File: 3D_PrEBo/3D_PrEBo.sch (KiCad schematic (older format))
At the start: 69 parts, among them J1 LED, J10 FAN&LED_INPUT, J11 TMC_INPUT, J12 Fan_interconnection_header, J13 Conn_01x04, J14 Conn_01x03, J2 RJ45, J3 X, J4 Y, J5 Z, J6 E0, J7 E1, J9 X_endstop, M1 Fan_3pin, M2 Fan_3pin, M3 Fan_3pin, M4 Fan_3pin, M5 Fan_3pin, M6 Fan_3pin, M7 Fan_3pin, M8 Fan_4pin, Q1 AOD4189, Q10 IRLML2502, Q2 IRLML2502, Q3 IRLML2502, Q4 IRLML2502, Q5 IRLML2502, Q6 IRLML2502, Q7 IRLML2502, Q8 IRLML2502, Q9 IRLML2502, U1 L5973D, U2 NCP1117-5.0_SOT223

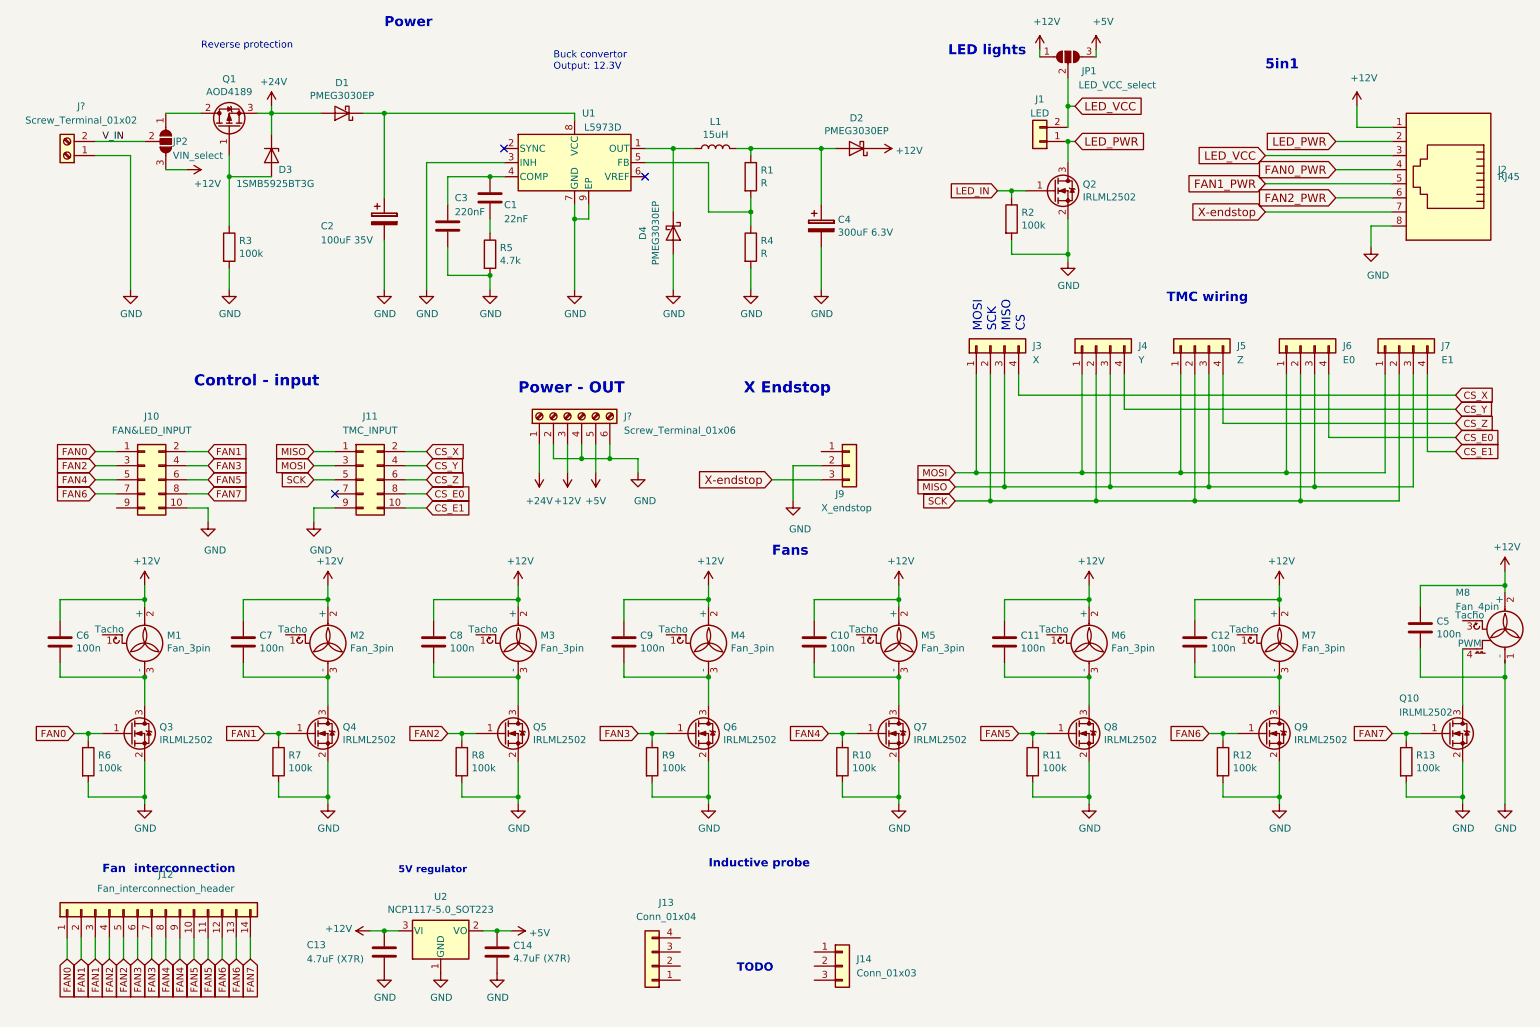
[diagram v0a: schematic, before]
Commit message: Schematic: Add inductive probe and set voltage of buck converter
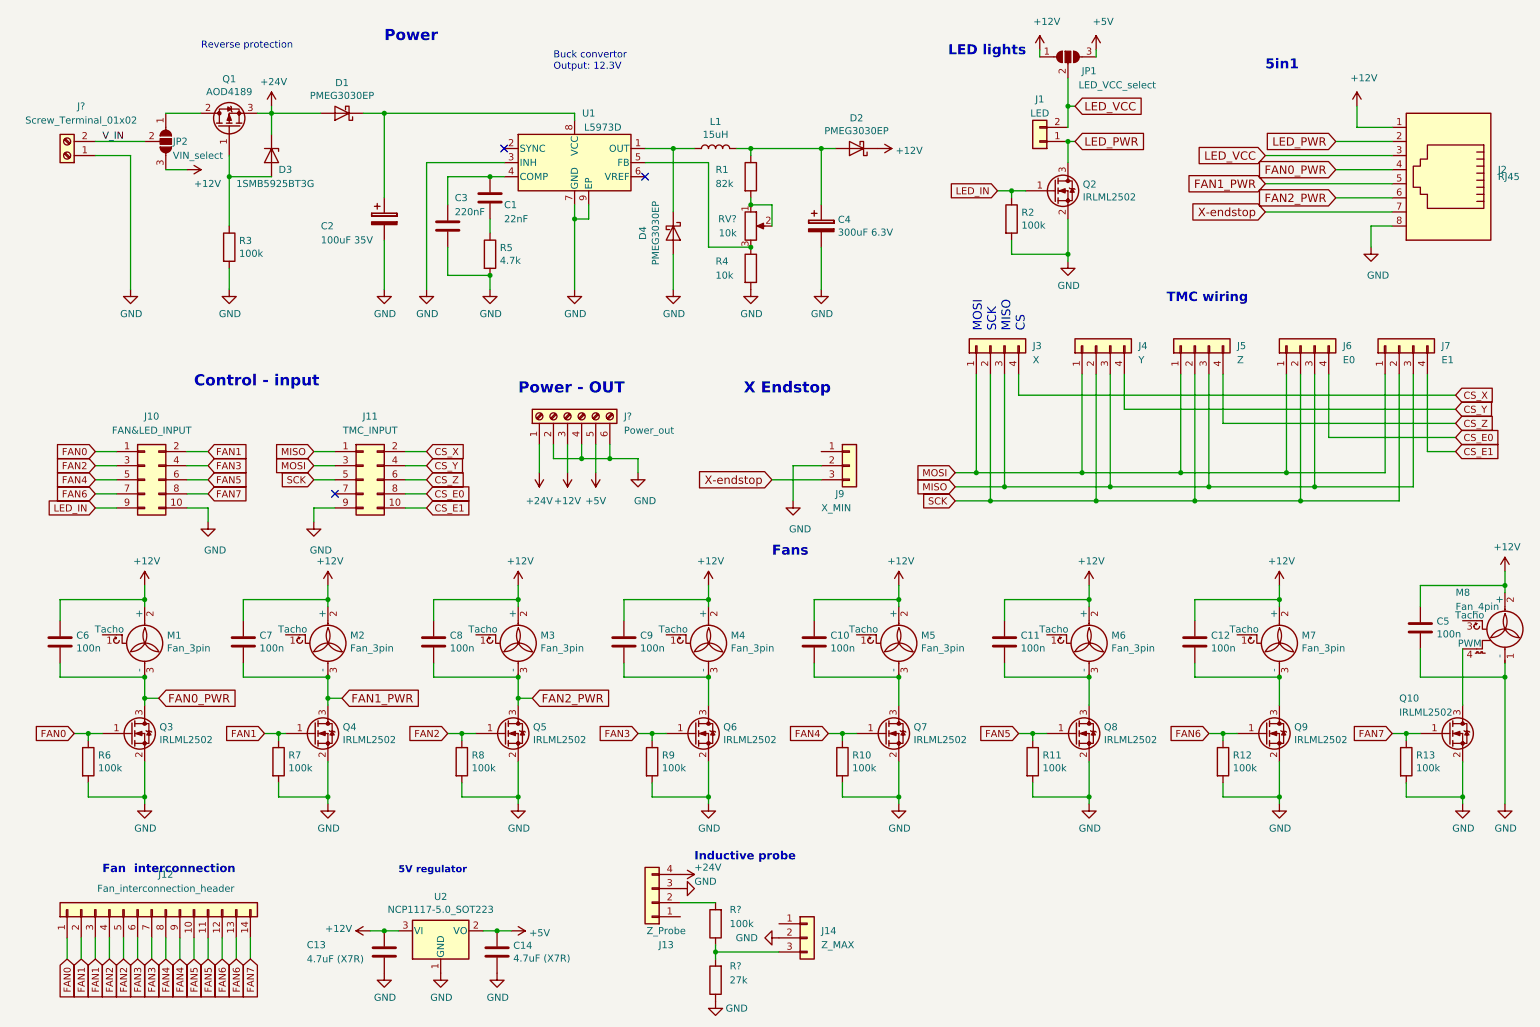
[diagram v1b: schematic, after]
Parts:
- added R?: 100k, symbol Device:R
- added R?: 27k, symbol Device:R
- added RV?: 10k, symbol Device:R_POT
- J13: value Conn_01x04 -> Z_Probe
- J14: value Conn_01x03 -> Z_MAX
- J9: value X_endstop -> X_MIN
- J?: value Screw_Terminal_01x06 -> Power_out
- R1: value R -> 82k
- R4: value R -> 10k
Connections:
- net +24V: now also J13.4 (Pin_4)
- net FAN0_PWR: now also C6.2, M1.3 (-), Q3.3 (D)
- net FAN1_PWR: now also C7.2, M2.3 (-), Q4.3 (D)
- net FAN2_PWR: now also C8.2, M3.3 (-), Q5.3 (D)
- net GND: now also J13.3 (Pin_3), J14.2 (Pin_2), R?.1
- net LED_IN: now also J10.9 (Pin_9)
- net at R4.1, U1.5 (FB): now also RV?.3; no longer R1.2
- net at J13.2 (Pin_2): now also R?.2
- net at J14.3 (Pin_3): now also R?.1, R?.2
- new net: R1.2, RV?.1, RV?.2
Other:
- note removed: "TODO"
- moved on the sheet: J13, J14, R4
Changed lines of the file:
@@
 EESchema Schematic File Version 4
+LIBS:3D_PrEBo-cache
 EELAYER 26 0
 EELAYER END
@@
 encoding utf-8
 Sheet 1 1
-Title ""
-Date ""
-Rev ""
+Title "3D Printer expansion board"
+Date "2019-02-06"
+Rev "1.0"
 Comp ""
 Comment1 ""
@@
 U 1 1 5C5ABFEB
 P 5650 1750
-F 0 "R1" H 5720 1796 50  0000 L CNN
-F 1 "R" H 5720 1705 50  0000 L CNN
+F 0 "R1" H 5400 1800 50  0000 L CNN
+F 1 "82k" H 5400 1700 50  0000 L CNN
 F 2 "Resistor_SMD:R_0603_1608Metric" V 5580 1750 50  0001 C CNN
 F 3 "~" H 5650 1750 50  0001 C CNN
@@
 L Device:R R4
 U 1 1 5C5ABFF2
-P 5650 2250
-F 0 "R4" H 5720 2296 50  0000 L CNN
-F 1 "R" H 5720 2205 50  0000 L CNN
-F 2 "Resistor_SMD:R_0603_1608Metric" V 5580 2250 50  0001 C CNN
-F 3 "~" H 5650 2250 50  0001 C CNN
-	1    5650 2250
+P 5650 2400
+F 0 "R4" H 5400 2450 50  0000 L CNN
+F 1 "10k" H 5400 2350 50  0000 L CNN
+F 2 "Resistor_SMD:R_0603_1608Metric" V 5580 2400 50  0001 C CNN
+F 3 "~" H 5650 2400 50  0001 C CNN
+	1    5650 2400
 	1    0    0    -1
 $EndComp
@@
 	5100 2300 5100 2550
 Wire Wire Line
-	5650 2100 5650 2000
-Wire Wire Line
-	5650 2000 5350 2000
-Wire Wire Line
-	5350 2000 5350 1650
-Wire Wire Line
 	5350 1650 4900 1650
-Connection ~ 5650 2000
-Wire Wire Line
-	5650 2000 5650 1900
 Wire Wire Line
 	5650 1600 5650 1550
-Wire Wire Line
-	5650 2400 5650 2550
 $Comp
 L power:GND #PWR0106
@@
 	950  6050 950  6150
 Wire Wire Line
-	1350 5300 1350 5500
+	1350 5300 1350 5450
 Connection ~ 1350 5300
 $Comp
@@
 	2300 6050 2300 6150
 Wire Wire Line
-	2650 5300 2650 5500
+	2650 5300 2650 5450
 Connection ~ 2650 5300
 Wire Wire Line
@@
 	3600 6050 3600 6150
 Wire Wire Line
-	4000 5300 4000 5500
+	4000 5300 4000 5450
 Connection ~ 4000 5300
 $Comp
@@
 L Connector_Generic:Conn_01x04 J13
 U 1 1 5C784DB9
-P 4950 7350
-F 0 "J13" H 4850 6900 50  0000 C CNN
-F 1 "Conn_01x04" H 4850 7000 50  0000 C CNN
-F 2 "" H 4950 7350 50  0001 C CNN
-F 3 "~" H 4950 7350 50  0001 C CNN
-	1    4950 7350
+P 4950 6900
+F 0 "J13" H 4850 7200 50  0000 C CNN
+F 1 "Z_Probe" H 4850 7100 50  0000 C CNN
+F 2 "" H 4950 6900 50  0001 C CNN
+F 3 "~" H 4950 6900 50  0001 C CNN
+	1    4950 6900
 	-1   0    0    1
 $EndComp
@@
 L Connector_Generic:Conn_01x03 J14
 U 1 1 5C78508D
-P 6300 7350
-F 0 "J14" H 6400 7400 50  0000 L CNN
-F 1 "Conn_01x03" H 6400 7300 50  0000 L CNN
-F 2 "" H 6300 7350 50  0001 C CNN
-F 3 "~" H 6300 7350 50  0001 C CNN
-	1    6300 7350
-	1    0    0    -1
-$EndComp
-Text Notes 5350 6850 0    59   ~ 12
+P 6050 7150
+F 0 "J14" H 6150 7200 50  0000 L CNN
+F 1 "Z_MAX" H 6150 7100 50  0000 L CNN
+F 2 "" H 6050 7150 50  0001 C CNN
+F 3 "~" H 6050 7150 50  0001 C CNN
+	1    6050 7150
+	1    0    0    -1
+$EndComp
+Text Notes 5250 6800 0    59   ~ 12
 Inductive probe\n\n\n
 $Comp
@@
 Text Notes 5800 4450 0    71   ~ 14
 Fans
-Text Notes 3050 700  0    71   ~ 14
+Text Notes 3050 800  0    79   ~ 16
 Power
 Text Notes 9300 1000 0    71   ~ 14
@@
 P 6350 3800
 F 0 "J9" H 6250 3600 50  0000 L CNN
-F 1 "X_endstop" H 6150 3500 50  0000 L CNN
+F 1 "X_MIN" H 6150 3500 50  0000 L CNN
 F 2 "" H 6350 3800 50  0001 C CNN
 F 3 "~" H 6350 3800 50  0001 C CNN
@@
 P 4350 3450
 F 0 "J?" V 4350 3050 50  0000 R CNN
-F 1 "Screw_Terminal_01x06" V 4250 3050 50  0000 R CNN
+F 1 "Power_out" V 4250 3050 50  0000 R CNN
 F 2 "" H 4350 3450 50  0001 C CNN
 F 3 "~" H 4350 3450 50  0001 C CNN
@@
 Wire Wire Line
 	1500 1300 1750 1300
-Text Notes 5550 7400 0    59   ~ 12
-TODO
+$Comp
+L power:+24V #PWR?
+U 1 1 5C5C5730
+P 5150 6700
+F 0 "#PWR?" H 5150 6550 50  0001 C CNN
+F 1 "+24V" V 5100 6800 50  0000 L CNN
+F 2 "" H 5150 6700 50  0001 C CNN
+F 3 "" H 5150 6700 50  0001 C CNN
+	1    5150 6700
+	0    1    1    0
+$EndComp
+$Comp
+L power:GND #PWR?
+U 1 1 5C5C5890
+P 5150 6800
+F 0 "#PWR?" H 5150 6550 50  0001 C CNN
+F 1 "GND" V 5200 6700 50  0000 R CNN
+F 2 "" H 5150 6800 50  0001 C CNN
+F 3 "" H 5150 6800 50  0001 C CNN
+	1    5150 6800
+	0    -1   -1   0
+$EndComp
+$Comp
+L Device:R R?
+U 1 1 5C5C5B28
+P 5400 7050
+F 0 "R?" H 5300 6950 50  0000 R CNN
+F 1 "100k" H 5300 7050 50  0000 R CNN
+F 2 "" V 5330 7050 50  0001 C CNN
+F 3 "~" H 5400 7050 50  0001 C CNN
+	1    5400 7050
+	-1   0    0    1
+$EndComp
+$Comp
+L Device:R R?
+U 1 1 5C5DA2B6
+P 5400 7450
+F 0 "R?" H 5300 7350 50  0000 R CNN
+F 1 "27k" H 5300 7450 50  0000 R CNN
+F 2 "" V 5330 7450 50  0001 C CNN
+F 3 "~" H 5400 7450 50  0001 C CNN
+	1    5400 7450
+	-1   0    0    1
+$EndComp
+Wire Wire Line
+	5400 6900 5150 6900
+$Comp
+L power:GND #PWR?
+U 1 1 5C6418C9
+P 5400 7600
+F 0 "#PWR?" H 5400 7350 50  0001 C CNN
+F 1 "GND" H 5550 7550 50  0000 C CNN
+F 2 "" H 5400 7600 50  0001 C CNN
+F 3 "" H 5400 7600 50  0001 C CNN
+	1    5400 7600
+	1    0    0    -1
+$EndComp
+Wire Wire Line
+	5400 7200 5400 7250
+Wire Wire Line
+	5400 7250 5850 7250
+Connection ~ 5400 7250
+Wire Wire Line
+	5400 7250 5400 7300
+$Comp
+L power:GND #PWR?
+U 1 1 5C71260A
+P 5850 7150
+F 0 "#PWR?" H 5850 6900 50  0001 C CNN
+F 1 "GND" V 5850 7000 50  0000 R CNN
+F 2 "" H 5850 7150 50  0001 C CNN
+F 3 "" H 5850 7150 50  0001 C CNN
+	1    5850 7150
+	0    1    1    0
+$EndComp
+Text GLabel 1450 5450 2    59   Input ~ 0
+FAN0_PWR
+Wire Wire Line
+	1450 5450 1350 5450
+Connection ~ 1350 5450
+Wire Wire Line
+	1350 5450 1350 5500
+Text GLabel 2750 5450 2    59   Input ~ 0
+FAN1_PWR
+Wire Wire Line
+	2750 5450 2650 5450
+Connection ~ 2650 5450
+Wire Wire Line
+	2650 5450 2650 5500
+Text GLabel 4100 5450 2    59   Input ~ 0
+FAN2_PWR
+Wire Wire Line
+	4100 5450 4000 5450
+Connection ~ 4000 5450
+Wire Wire Line
+	4000 5450 4000 5500
+Wire Wire Line
+	5650 2250 5350 2250
+Wire Wire Line
+	5350 1650 5350 2250
+Wire Wire Line
+	5650 1900 5650 1950
+Connection ~ 5650 2250
+$Comp
+L Device:R_POT RV?
+U 1 1 5C76DB12
+P 5650 2100
+F 0 "RV?" H 5550 2150 50  0000 R CNN
+F 1 "10k" H 5550 2050 50  0000 R CNN
+F 2 "" H 5650 2100 50  0001 C CNN
+F 3 "~" H 5650 2100 50  0001 C CNN
+	1    5650 2100
+	1    0    0    -1
+$EndComp
+Wire Wire Line
+	5650 1950 5800 1950
+Wire Wire Line
+	5800 1950 5800 2100
+Connection ~ 5650 1950
+Text GLabel 1000 4100 0    50   Input ~ 0
+LED_IN
+Wire Wire Line
+	1000 4100 1150 4100
 $EndSCHEMATC
